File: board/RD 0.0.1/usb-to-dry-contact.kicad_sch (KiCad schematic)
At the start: 28 parts, among them J1 480-37-1000, J2 CONN_OUT, J4 CONN_SWIM, K2 G5V-1, Q1 IRLML0030, U1 CP2102N-Axx-xQFN28, U2 STM8S003F3P

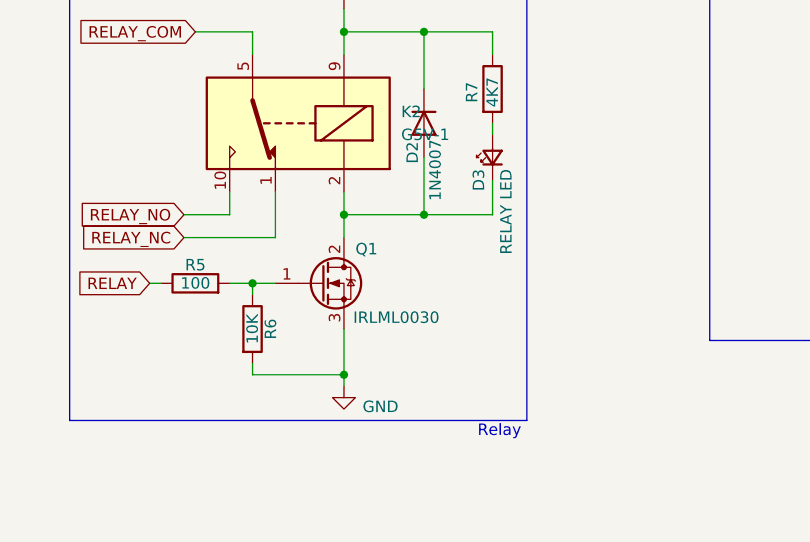
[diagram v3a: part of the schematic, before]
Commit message: Change wrong symbol for the Relay MOSFET
The symbol has switched Drain pin and Source pin
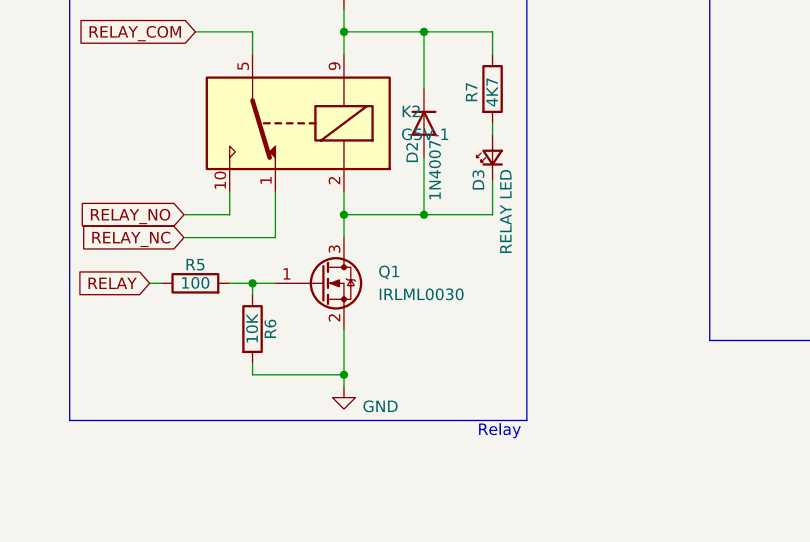
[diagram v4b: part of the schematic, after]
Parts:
- removed Q1: IRLML0030, Package_TO_SOT_SMD:SOT-23, symbol Transistor_FET:IRF540N
- added Q1: IRLML0030, Package_TO_SOT_SMD:SOT-23, symbol Transistor_FET:IRLML0030
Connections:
- net GND: now also Q1.2 (S)
- net at R5.2, R6.1: now also Q1.1 (G)
- net at D2.2 (A), D3.1 (K), K2.2: now also Q1.3 (D)
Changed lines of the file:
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@@
-	)
-	(symbol
-		(lib_id "Transistor_FET:IRF540N")
-		(at 59.69 115.57 0)
-		(unit 1)
-		(exclude_from_sim no)
-		(in_bom yes)
-		(on_board yes)
-		(dnp no)
-		(property "Reference" "Q1"
-			(at 63.5 111.76 0)
-			(effects
-				(font
-					(size 1.27 1.27)
-				)
-				(justify left)
-			)
-		)
-		(property "Value" "IRLML0030"
-			(at 63.246 119.38 0)
-			(effects
-				(font
-					(size 1.27 1.27)
-				)
-				(justify left)
-			)
-		)
-		(property "Footprint" "Package_TO_SOT_SMD:SOT-23"
-			(at 64.77 117.475 0)
-			(effects
-				(font
-					(size 1.27 1.27)
-					(italic yes)
-				)
-				(justify left)
-				(hide yes)
-			)
-		)
-		(property "Datasheet" ""
-			(at 64.77 119.38 0)
-			(effects
-				(font
-					(size 1.27 1.27)
-				)
-				(justify left)
-				(hide yes)
-			)
-		)
-		(property "Description" ""
-			(at 59.69 115.57 0)
-			(effects
-				(font
-					(size 1.27 1.27)
-				)
-				(hide yes)
-			)
-		)
-		(property "Manufacturer" "Infineon Technologies"
-			(at 59.69 115.57 0)
-			(effects
-				(font
-					(size 1.27 1.27)
-				)
-				(hide yes)
-			)
-		)
-		(property "Mfg PN" "IRLML0030TRPBF "
-			(at 59.69 115.57 0)
-			(effects
-				(font
-					(size 1.27 1.27)
-				)
-				(hide yes)
-			)
-		)
-		(property "Availability" ""
-			(at 59.69 115.57 0)
-			(effects
-				(font
-					(size 1.27 1.27)
-				)
-				(hide yes)
-			)
-		)
-		(property "CUI_purchase_URL" ""
-			(at 59.69 115.57 0)
-			(effects
-				(font
-					(size 1.27 1.27)
-				)
-				(hide yes)
-			)
-		)
-		(property "Check_prices" ""
-			(at 59.69 115.57 0)
-			(effects
-				(font
-					(size 1.27 1.27)
-				)
-				(hide yes)
-			)
-		)
-		(property "Description_1" ""
-			(at 59.69 115.57 0)
-			(effects
-				(font
-					(size 1.27 1.27)
-				)
-				(hide yes)
-			)
-		)
-		(property "MF" ""
-			(at 59.69 115.57 0)
-			(effects
-				(font
-					(size 1.27 1.27)
-				)
-				(hide yes)
-			)
-		)
-		(property "MP" ""
-			(at 59.69 115.57 0)
-			(effects
-				(font
-					(size 1.27 1.27)
-				)
-				(hide yes)
-			)
-		)
-		(property "Package" ""
-			(at 59.69 115.57 0)
-			(effects
-				(font
-					(size 1.27 1.27)
-				)
-				(hide yes)
-			)
-		)
-		(property "Price" ""
-			(at 59.69 115.57 0)
-			(effects
-				(font
-					(size 1.27 1.27)
-				)
-				(hide yes)
-			)
-		)
-		(property "STANDARD" ""
-			(at 59.69 115.57 0)
-			(effects
-				(font
-					(size 1.27 1.27)
-				)
-				(hide yes)
-			)
-		)
-		(property "SnapEDA_Link" ""
-			(at 59.69 115.57 0)
-			(effects
-				(font
-					(size 1.27 1.27)
-				)
-				(hide yes)
-			)
-		)
-		(property "LCSC Part #" "C67272"
-			(at 59.69 115.57 0)
-			(effects
-				(font
-					(size 1.27 1.27)
-				)
-				(hide yes)
-			)
-		)
-		(property "LCSC PN" ""
-			(at 59.69 115.57 0)
-			(effects
-				(font
-					(size 1.27 1.27)
-				)
-				(hide yes)
-			)
-		)
-		(pin "2"
-		)
-		(pin "3"
-		)
-		(pin "1"
-		)
-		(instances
-			(project "usb-to-dry-contact"
-				(path "/42c637e2-fe5f-4695-b5f1-9c2d3cf27872"
-					(reference "Q1")
-					(unit 1)
-				)
-			)
-		)
 	)
 	(symbol
@@
 					(unit 1)
 				)
+			)
+		)
+	)
+	(symbol
+		(lib_id "Transistor_FET:IRLML0030")
+		(at 59.69 115.57 0)
+		(unit 1)
+		(exclude_from_sim no)
+		(in_bom yes)
+		(on_board yes)
+		(dnp no)
+		(fields_autoplaced yes)
+		(property "Reference" "Q1"
+			(at 66.04 114.2999 0)
+			(effects
+				(font
+					(size 1.27 1.27)
+				)
+				(justify left)
+			)
+		)
+		(property "Value" "IRLML0030"
+			(at 66.04 116.8399 0)
+			(effects
+				(font
+					(size 1.27 1.27)
+				)
+				(justify left)
+			)
+		)
+		(property "Footprint" "Package_TO_SOT_SMD:SOT-23"
+			(at 64.77 117.475 0)
+			(effects
+				(font
+					(size 1.27 1.27)
+					(italic yes)
+				)
+				(justify left)
+				(hide yes)
+			)
+		)
+		(property "Datasheet" "https://www.infineon.com/dgdl/irlml0030pbf.pdf?fileId=5546d462533600a401535664773825df"
+			(at 64.77 119.38 0)
+			(effects
+				(font
+					(size 1.27 1.27)
+				)
+				(justify left)
+				(hide yes)
+			)
+		)
+		(property "Description" "5.3A Id, 30V Vds, 27mOhm Rds, N-Channel HEXFET Power MOSFET, SOT-23"
+			(at 59.69 115.57 0)
+			(effects
+				(font
+					(size 1.27 1.27)
+				)
+				(hide yes)
+			)
+		)
+		(property "LCSC Part #" "C67272"
+			(at 59.69 115.57 0)
+			(effects
+				(font
+					(size 1.27 1.27)
+				)
+				(hide yes)
+			)
+		)
+		(property "Mfg PN" "IRLML0030TRPBF "
+			(at 59.69 115.57 0)
+			(effects
+				(font
+					(size 1.27 1.27)
+				)
+				(hide yes)
+			)
+		)
+		(pin "3"
+		)
+		(pin "1"
+		)
+		(pin "2"
+		)
+		(instances
+			(project ""
+				(path "/42c637e2-fe5f-4695-b5f1-9c2d3cf27872"
+					(reference "Q1")
+					(unit 1)
+				)
